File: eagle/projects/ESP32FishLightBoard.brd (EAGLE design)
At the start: 69.8 x 30.5 mm, 9 parts, among them U1 SN74HCT04N

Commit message: updated to v1.1 PCB
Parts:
- added BZR: F/QMX, buzzer:F/QMX
- added OLED: 22-27-2041-04, con-molex:6410-04
- added T3V3, TDAT, TGND: WIREPAD2,54/1,0, wirepad:2,54/1,0
- moved C1 23.3 mm to (75.7, 12.1), turned to 180 degrees
- moved VCC 22.9 mm to (73.7, 7.08), turned to 270 degrees
- moved R1 21.3 mm to (36.8, 23.2), turned to 180 degrees
- moved GND 21.2 mm to (77.5, 7.08), turned to 270 degrees
- moved LVCC 7.28 mm to (68.9, 7.08), turned to 270 degrees
- moved U$1 5.73 mm to (31.9, 17.9)
- moved LGND 4.70 mm to (61.3, 7.08), turned to 270 degrees
- moved LDAT 2.97 mm to (65.1, 7.08), turned to 270 degrees
- moved U1 0.45 mm to (30.1, 11.5)
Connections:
- new net 3V3: OLED.2, T3V3.1, U$1.1
- new net IO12: U$1.13
- new net IO14: U$1.12
- new net IO15: BZR.+, U$1.23
- new net IO16: TDAT.1, U$1.27
- new net SCL: OLED.3, U$1.36
- new net SDA: OLED.4, U$1.33
- net GND: now also BZR.-, OLED.1, TGND.1
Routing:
- net 3V3: track 0.00 -> 87.8 mm
- net IO16: track 0.00 -> 48.8 mm
- net SDA: track 0.00 -> 27.4 mm
- net VCC: track 53.3 -> 38.9 mm
- net IO15: track 0.00 -> 14.0 mm
- net SCL: track 0.00 -> 13.9 mm
- net IO17: track 27.0 -> 16.2 mm
- net IO17+: track 29.4 -> 32.4 mm
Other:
- board size 69.8 x 30.5 mm -> 81.3 x 35.6 mm
- board text added: "Fish-Light-Control v1.1"
- board text removed: "Fish-Light-Control v1.0"

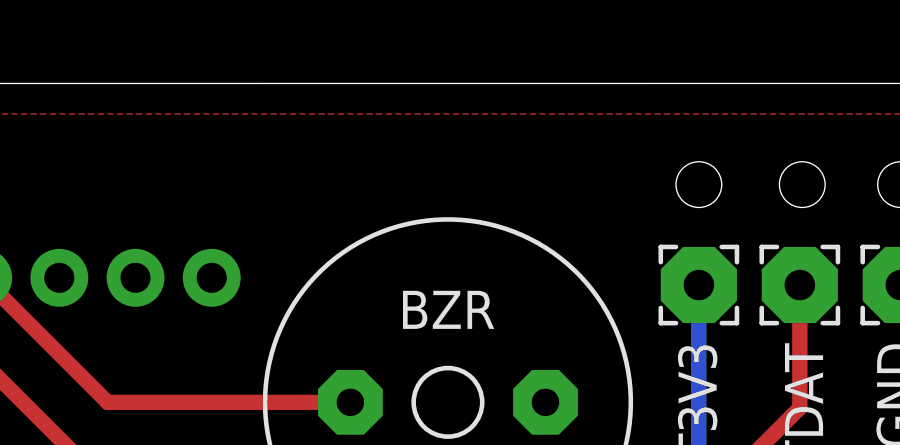
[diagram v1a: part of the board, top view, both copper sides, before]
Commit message: Adding eagle for v1.1 board
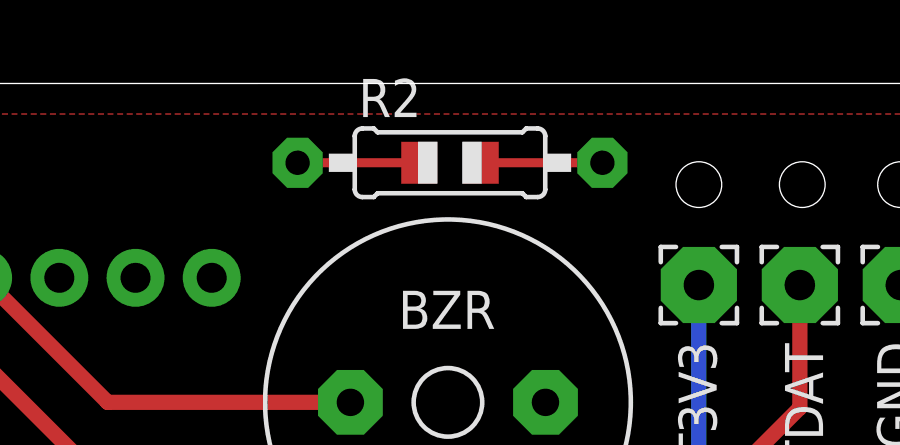
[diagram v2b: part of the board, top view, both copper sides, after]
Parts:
- added R2: 4.7k, adafruit:0805-THM
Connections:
- net 3V3: now also R2.2
- net IO16: now also R2.1
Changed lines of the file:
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@@
 <drawing>
 <settings>
-<setting alwaysvectorfont="yes"/>
+<setting alwaysvectorfont="no"/>
 <setting verticaltext="up"/>
 </settings>
@@
 </layers>
 <board>
-<fusionsync huburn="a.cGVyc29uYWw6dWUyZGU1ODA1" projecturn="a.cGVyc29uYWw6dWUyZGU1ODA1IzIwMTgwNjEyMTM1ODcyNjAx" f3durn="urn:adsk.wipprod:dm.lineage:z2O6571GQPCz1NHR0V4pvg" pcbguid="" lastpulledtime="" lastsyncedchangeguid="" latestrevisionid="596e750d-dbe9-4d4d-a9ff-1baaa34a1126" lastsyncedrevisionid="596e750d-dbe9-4d4d-a9ff-1baaa34a1126" lastboardhashguid="47ef04cf-4adc-7d94-b231-991cd53c54a2" lastpushedtime="2021-02-21T03:09:37Z" linktopcb3d="true"/>
+<fusionsync huburn="a.cGVyc29uYWw6dWUyZGU1ODA1" projecturn="a.cGVyc29uYWw6dWUyZGU1ODA1IzIwMTgwNjEyMTM1ODcyNjAx" f3durn="urn:adsk.wipprod:dm.lineage:z2O6571GQPCz1NHR0V4pvg" pcbguid="" lastpulledtime="" lastsyncedchangeguid="" latestrevisionid="596e750d-dbe9-4d4d-a9ff-1baaa34a1126" lastsyncedrevisionid="596e750d-dbe9-4d4d-a9ff-1baaa34a1126" lastboardhashguid="47ef04cf-4adc-7d94-b231-991cd53c54a2" lastpushedtime="2021-02-21T03:09:37Z" linktopcb3d="false"/>
 <plain>
 <hole x="65.0868625" y="3.614421875" drill="1.524"/>
@@
 <attribute name="POPULARITY" value="0" x="4.404359375" y="17.901921875" size="1.778" layer="27" rot="R270" display="off"/>
 </element>
+<element name="R2" library="adafruit" library_urn="urn:adsk.eagle:library:420" package="0805-THM" package3d_urn="urn:adsk.eagle:package:6240726/1" value="4.7k" x="62.682121875" y="32.918396875" smashed="yes">
+<attribute name="NAME" x="59.634121875" y="34.442396875" size="1.27" layer="25" ratio="10"/>
+<attribute name="VALUE" x="59.551521875" y="30.143396875" size="1.27" layer="27" ratio="10"/>
+</element>
 </elements>
 <signals>
@@
 <wire x1="55.275475" y1="18.112740625" x2="45.87239375" y2="27.515821875" width="0.508" layer="1"/>
 <wire x1="45.87239375" y1="27.515821875" x2="38.5275375" y2="27.515821875" width="0.508" layer="1"/>
+<contactref element="R2" pad="1"/>
+<wire x1="57.602121875" y1="32.918396875" x2="36.9597" y2="29.083659375" width="0" layer="19" extent="1-1"/>
 </signal>
 <signal name="3V3">
@@
 <wire x1="6.482078125" y1="16.631921875" x2="4.404359375" y2="16.631921875" width="0.508" layer="16"/>
 <wire x1="9.0197" y1="14.0943" x2="6.482078125" y2="16.631921875" width="0.508" layer="16"/>
+<contactref element="R2" pad="2"/>
+<wire x1="67.762121875" y1="32.918396875" x2="9.0197" y2="6.433659375" width="0" layer="19" extent="1-1"/>
 </signal>
 <signal name="IO15">
